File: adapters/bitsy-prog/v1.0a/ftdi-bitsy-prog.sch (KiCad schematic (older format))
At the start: 4 parts, among them J1 Conn, J2 CS, J3 GND, J4 Prog

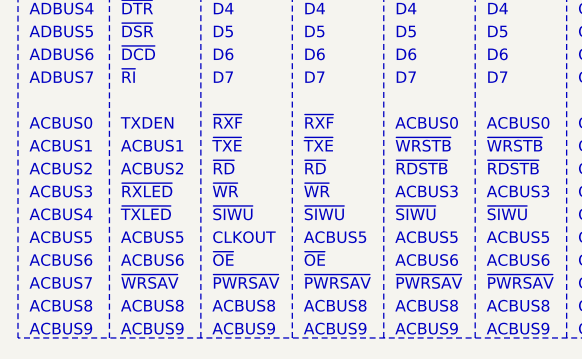
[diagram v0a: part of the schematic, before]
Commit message: A bunch of minor fixes.
* PWRSAV instead of WRSAV in signal table.
* 0.05 solder stop opening instead of 0.2
* Better copper fill parameters.
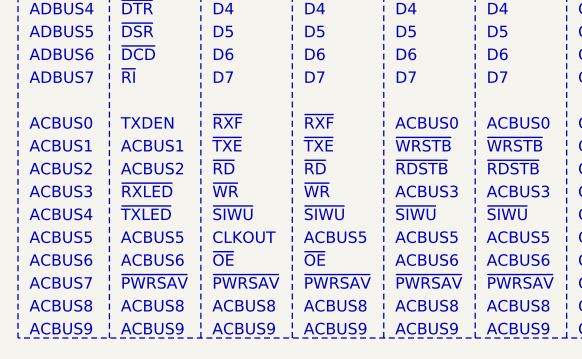
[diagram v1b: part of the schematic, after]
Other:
- note removed: "~WRSAV"
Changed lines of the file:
@@
 ACBUS8
 Text Notes 2450 5150 0    50   ~ 0
-~WRSAV
+~PWRSAV
 Text Notes 2450 5050 0    50   ~ 0
 ACBUS6
